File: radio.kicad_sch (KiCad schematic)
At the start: 4 parts

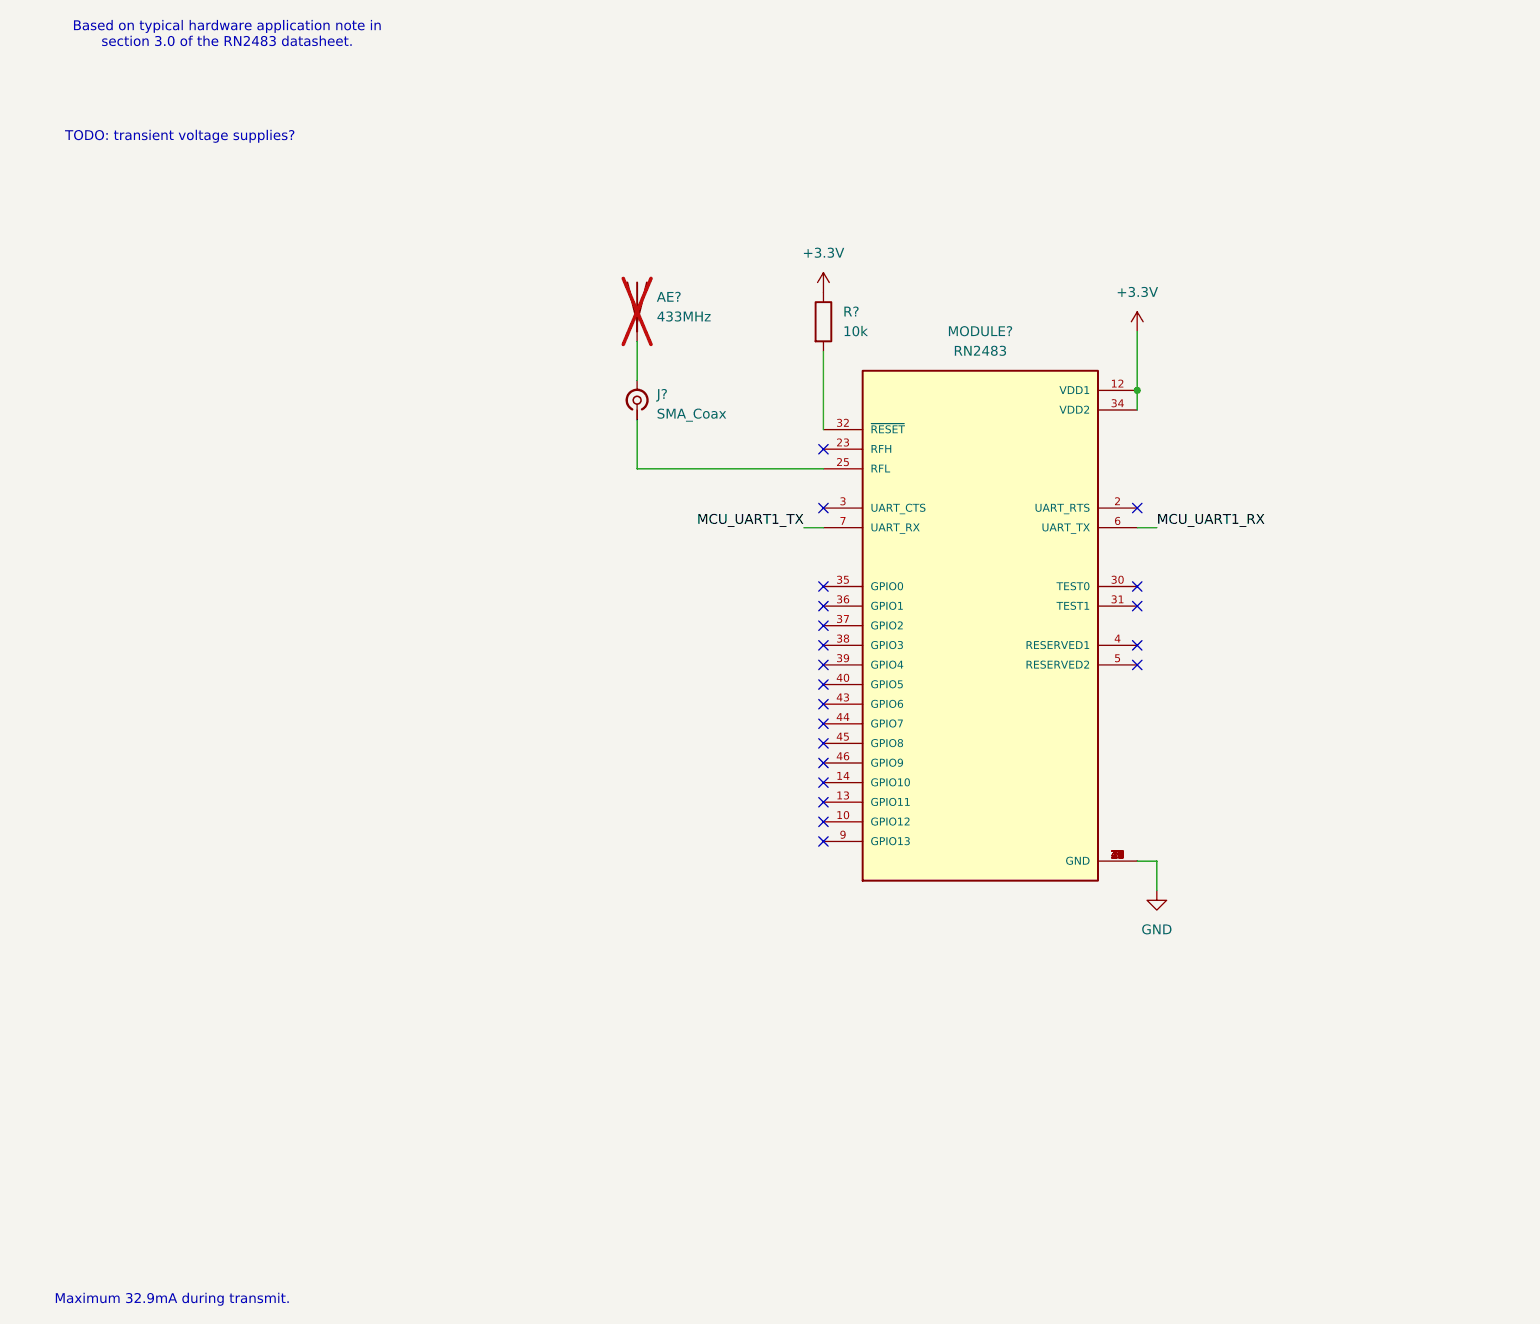
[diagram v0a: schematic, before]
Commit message: Added decoupling caps to RN2483 and fixed antenna connection. Also settled on easy GPS.
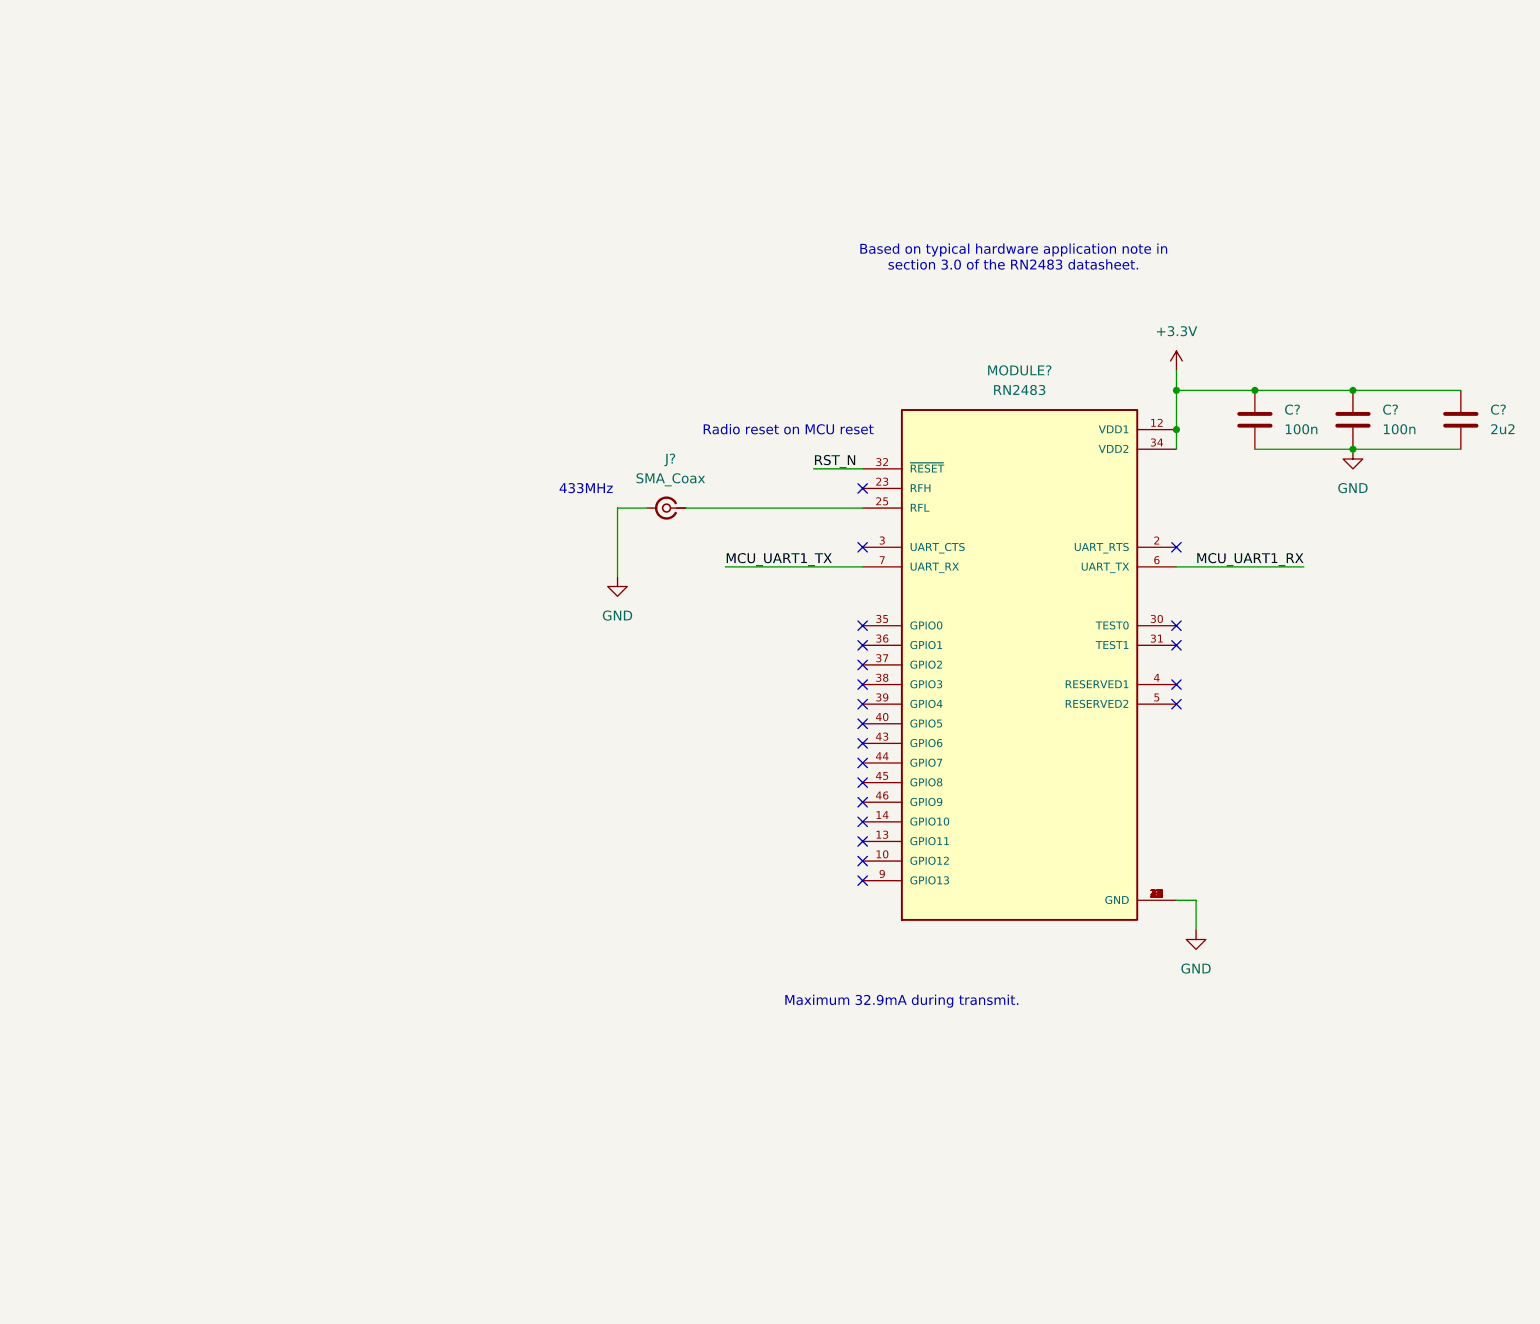
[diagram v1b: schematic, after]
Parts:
- removed AE?: 433MHz, symbol Device:Antenna
- removed R?: 10k, symbol Device:R
- added C?: 2u2, symbol Device:C
- added C? (x2): 100n, symbol Device:C
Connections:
- net +3.3V: now also C?.1, C?.1, C?.1
- net GND: now also J?.2 (Ext), C?.2, C?.2, C?.2
- net RST_N: now reaches MODULE?.32 (~{RESET})
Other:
- note added: "433MHz"
- note added: "Radio reset on MCU reset"
- note removed: "TODO: transient voltage supplies?"
- moved on the sheet: J?, MODULE?

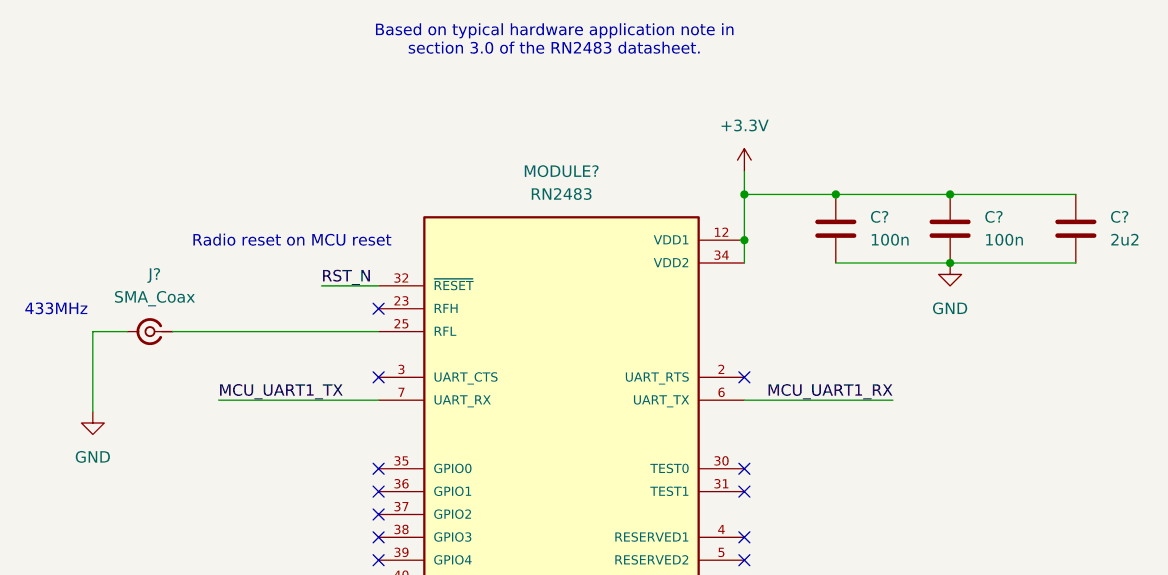
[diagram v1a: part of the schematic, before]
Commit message: Updated power supply to use buck regulator and power input MUX. Also computed current draw of the board to size power regulator.
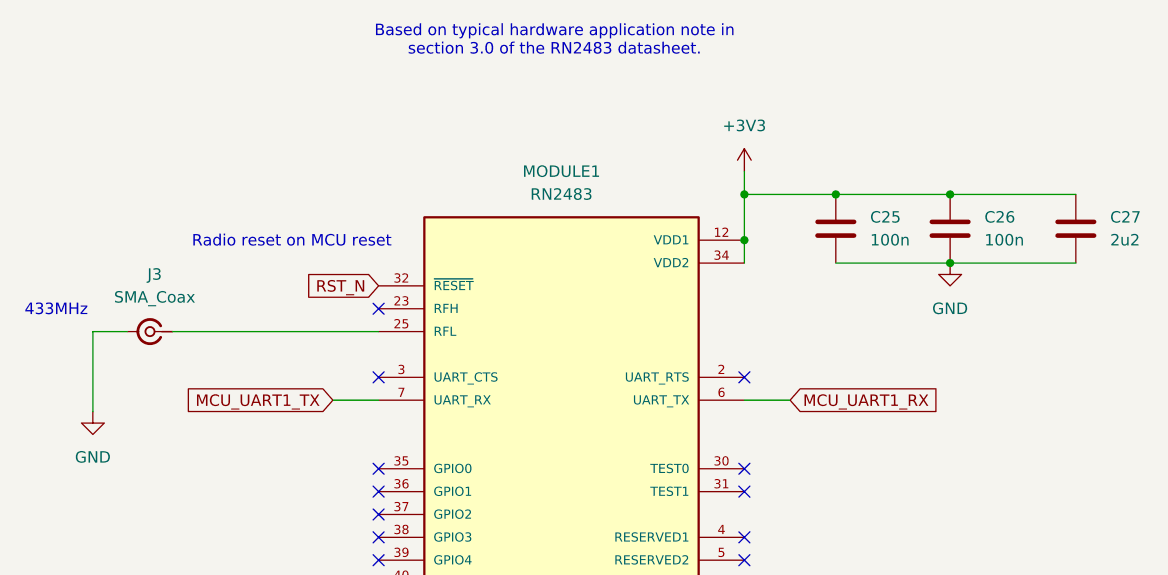
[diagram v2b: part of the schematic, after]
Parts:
- gave numbers to parts that had none: 5
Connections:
- net +3.3V renamed +3V3
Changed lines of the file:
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@@
+	(wire
+		(pts
+			(xy 172.72 92.71) (xy 167.64 92.71)
+		)
+		(stroke
+			(width 0)
+			(type default)
+		)
+	)
 	(wire
 		(pts
@@
 	(wire
 		(pts
+			(xy 121.92 92.71) (xy 127 92.71)
+		)
+		(stroke
+			(width 0)
+			(type default)
+		)
+	)
+	(wire
+		(pts
 			(xy 190.5 77.47) (xy 204.47 77.47)
 		)
@@
 		(pts
 			(xy 167.64 67.31) (xy 167.64 69.85)
-		)
-		(stroke
-			(width 0)
-			(type default)
-		)
-	)
-	(wire
-		(pts
-			(xy 184.15 92.71) (xy 167.64 92.71)
-		)
-		(stroke
-			(width 0)
-			(type default)
-		)
-	)
-	(wire
-		(pts
-			(xy 109.22 92.71) (xy 127 92.71)
-		)
-		(stroke
-			(width 0)
-			(type default)
-		)
-	)
-	(wire
-		(pts
-			(xy 120.65 80.01) (xy 127 80.01)
 		)
 		(stroke
@@
 		)
 	)
-	(label "RST_N"
-		(at 120.65 80.01 0)
+	(global_label "MCU_UART1_TX"
+		(shape input)
+		(at 121.92 92.71 180)
 		(fields_autoplaced yes)
 		(effects
@@
 				(size 1.27 1.27)
 			)
-			(justify left bottom)
-		)
-	)
-	(label "MCU_UART1_RX"
-		(at 184.15 92.71 180)
+			(justify right)
+		)
+		(property "Intersheetrefs" "${INTERSHEET_REFS}"
+			(at 104.9044 92.71 0)
+			(effects
+				(font
+					(size 1.27 1.27)
+				)
+				(justify right)
+				(hide yes)
+			)
+		)
+	)
+	(global_label "RST_N"
+		(shape input)
+		(at 127 80.01 180)
 		(fields_autoplaced yes)
 		(effects
@@
 				(size 1.27 1.27)
 			)
-			(justify right bottom)
-		)
-	)
-	(label "MCU_UART1_TX"
-		(at 109.22 92.71 0)
+			(justify right)
+		)
+		(property "Intersheetrefs" "${INTERSHEET_REFS}"
+			(at 118.2696 80.01 0)
+			(effects
+				(font
+					(size 1.27 1.27)
+				)
+				(justify right)
+				(hide yes)
+			)
+		)
+	)
+	(global_label "MCU_UART1_RX"
+		(shape input)
+		(at 172.72 92.71 0)
 		(fields_autoplaced yes)
 		(effects
@@
 				(size 1.27 1.27)
 			)
-			(justify left bottom)
+			(justify left)
+		)
+		(property "Intersheetrefs" "${INTERSHEET_REFS}"
+			(at 190.038 92.71 0)
+			(effects
+				(font
+					(size 1.27 1.27)
+				)
+				(justify left)
+				(hide yes)
+			)
 		)
 	)
@@
 		(dnp no)
 		(fields_autoplaced yes)
-		(property "Reference" "#PWR067"
+		(property "Reference" "#PWR059"
 			(at 95.25 100.33 0)
 			(effects
@@
 			(project ""
 				(path "/b90d3133-97a4-4747-8a68-e80f353c7b97/4aee52ff-1633-42f1-aa90-3806408b7a97"
-					(reference "#PWR067")
+					(reference "#PWR059")
 					(unit 1)
 				)
@@
 		(dnp no)
 		(fields_autoplaced yes)
-		(property "Reference" "C?"
+		(property "Reference" "C27"
 			(at 208.28 72.3899 0)
 			(effects
@@
 			(project ""
 				(path "/b90d3133-97a4-4747-8a68-e80f353c7b97/4aee52ff-1633-42f1-aa90-3806408b7a97"
-					(reference "C?")
+					(reference "C27")
 					(unit 1)
 				)
@@
 		(dnp no)
 		(fields_autoplaced yes)
-		(property "Reference" "C?"
+		(property "Reference" "C25"
 			(at 181.61 72.3899 0)
 			(effects
@@
 			(project "flight-computer"
 				(path "/b90d3133-97a4-4747-8a68-e80f353c7b97/4aee52ff-1633-42f1-aa90-3806408b7a97"
-					(reference "C?")
+					(reference "C25")
 					(unit 1)
 				)
@@
 		(dnp no)
 		(fields_autoplaced yes)
-		(property "Reference" "MODULE?"
+		(property "Reference" "MODULE1"
 			(at 147.32 67.31 0)
 			(effects
@@
 			(project ""
 				(path "/b90d3133-97a4-4747-8a68-e80f353c7b97/4aee52ff-1633-42f1-aa90-3806408b7a97"
-					(reference "MODULE?")
+					(reference "MODULE1")
 					(unit 1)
 				)
@@
 		(dnp no)
 		(fields_autoplaced yes)
-		(property "Reference" "J?"
+		(property "Reference" "J3"
 			(at 102.1195 78.74 0)
 			(effects
@@
 			(project ""
 				(path "/b90d3133-97a4-4747-8a68-e80f353c7b97/4aee52ff-1633-42f1-aa90-3806408b7a97"
-					(reference "J?")
+					(reference "J3")
 					(unit 1)
 				)
@@
 		(dnp no)
 		(fields_autoplaced yes)
-		(property "Reference" "C?"
+		(property "Reference" "C26"
 			(at 194.31 72.3899 0)
 			(effects
@@
 			(project "flight-computer"
 				(path "/b90d3133-97a4-4747-8a68-e80f353c7b97/4aee52ff-1633-42f1-aa90-3806408b7a97"
-					(reference "C?")
+					(reference "C26")
 					(unit 1)
 				)
@@
 		(dnp no)
 		(fields_autoplaced yes)
-		(property "Reference" "#PWR011"
+		(property "Reference" "#PWR060"
 			(at 170.18 146.05 0)
 			(effects
@@
 			(project ""
 				(path "/b90d3133-97a4-4747-8a68-e80f353c7b97/4aee52ff-1633-42f1-aa90-3806408b7a97"
-					(reference "#PWR011")
+					(reference "#PWR060")
 					(unit 1)
 				)
@@
 		(dnp no)
 		(fields_autoplaced yes)
-		(property "Reference" "#PWR066"
+		(property "Reference" "#PWR058"
 			(at 190.5 83.82 0)
 			(effects
@@
 			(project ""
 				(path "/b90d3133-97a4-4747-8a68-e80f353c7b97/4aee52ff-1633-42f1-aa90-3806408b7a97"
-					(reference "#PWR066")
+					(reference "#PWR058")
 					(unit 1)
 				)
@@
 		(dnp no)
 		(fields_autoplaced yes)
-		(property "Reference" "#PWR013"
+		(property "Reference" "#PWR057"
 			(at 167.64 71.12 0)
 			(effects
@@
 			)
 		)
-		(property "Value" "+3.3V"
+		(property "Value" "+3V3"
 			(at 167.64 62.23 0)
 			(effects
@@
 			(project ""
 				(path "/b90d3133-97a4-4747-8a68-e80f353c7b97/4aee52ff-1633-42f1-aa90-3806408b7a97"
-					(reference "#PWR013")
+					(reference "#PWR057")
 					(unit 1)
 				)

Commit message: Added footprints for all components
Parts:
- C25, C26: footprint (none) -> Capacitor_SMD:C_0201_0603Metric
- C27: footprint (none) -> Capacitor_SMD:C_0603_1608Metric
- J3: footprint (none) -> Connector_Coaxial:SMA_Molex_73251-1153_EdgeMount_Horizontal
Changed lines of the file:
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@@
 			)
 		)
-		(property "Footprint" ""
+		(property "Footprint" "Capacitor_SMD:C_0603_1608Metric"
 			(at 205.4352 77.47 0)
 			(effects
@@
 			)
 		)
-		(property "Footprint" ""
+		(property "Footprint" "Capacitor_SMD:C_0201_0603Metric"
 			(at 178.7652 77.47 0)
 			(effects
@@
 			)
 		)
-		(property "Footprint" ""
+		(property "Footprint" "Connector_Coaxial:SMA_Molex_73251-1153_EdgeMount_Horizontal"
 			(at 101.6 85.09 0)
 			(effects
@@
 			)
 		)
-		(property "Footprint" ""
+		(property "Footprint" "Capacitor_SMD:C_0201_0603Metric"
 			(at 191.4652 77.47 0)
 			(effects

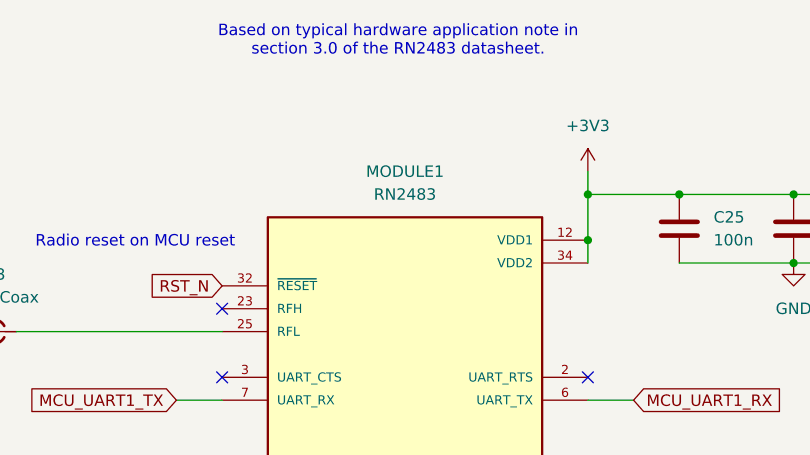
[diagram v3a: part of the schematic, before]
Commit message: Updated PCB so components are now on there.
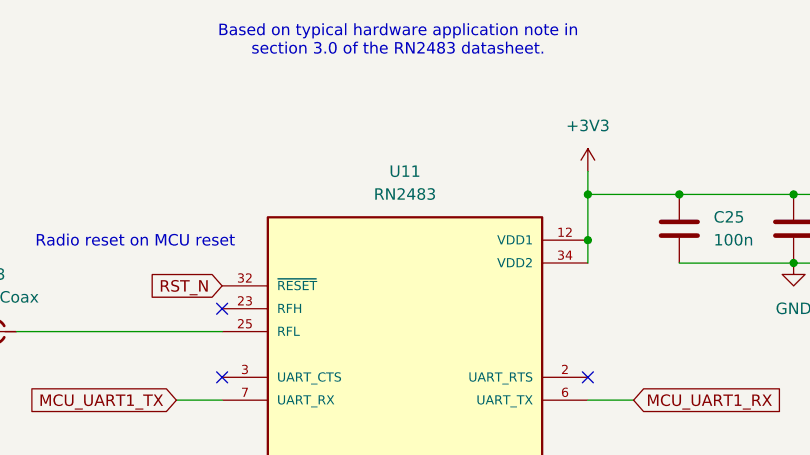
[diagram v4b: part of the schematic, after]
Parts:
- renumbered MODULE1 to U11
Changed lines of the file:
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@@
 		(dnp no)
 		(fields_autoplaced yes)
-		(property "Reference" "MODULE1"
+		(property "Reference" "U11"
 			(at 147.32 67.31 0)
 			(effects
@@
 			(project ""
 				(path "/b90d3133-97a4-4747-8a68-e80f353c7b97/4aee52ff-1633-42f1-aa90-3806408b7a97"
-					(reference "MODULE1")
+					(reference "U11")
 					(unit 1)
 				)
